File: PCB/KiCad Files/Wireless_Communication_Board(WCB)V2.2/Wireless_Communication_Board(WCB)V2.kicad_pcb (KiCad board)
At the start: 4 copper layers, 52.5 x 38.3 mm, 44 parts, among them J1 USB_B_Micro, J2 Power In, J3 Conn_01x04, J4 Conn_01x04, J5 Conn_01x04, J6 Conn_01x04, J7 Conn_01x04, Q2 UMH3N, U1 ESP32-PICO-MINI-02, U2 CP2102N-A02-GQFN28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

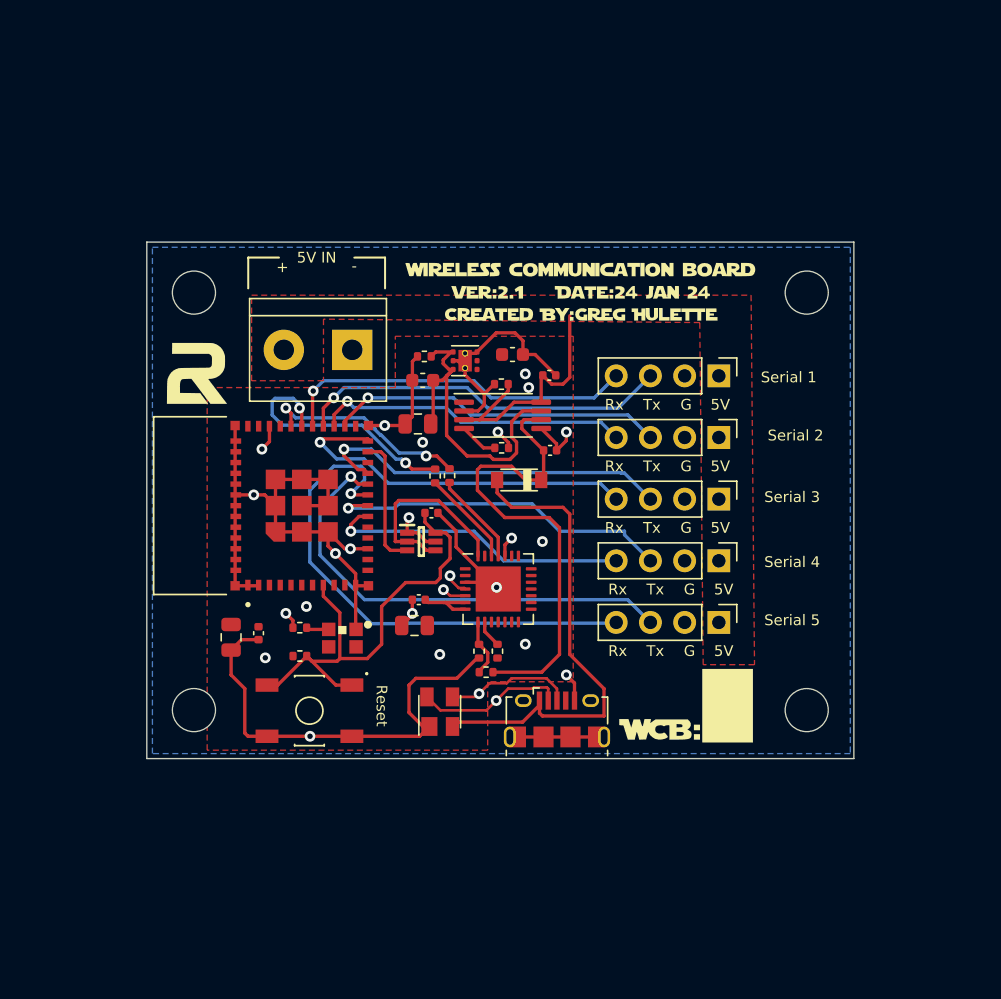
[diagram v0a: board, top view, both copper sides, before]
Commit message: Added WCB V2.2 and working on the code some.
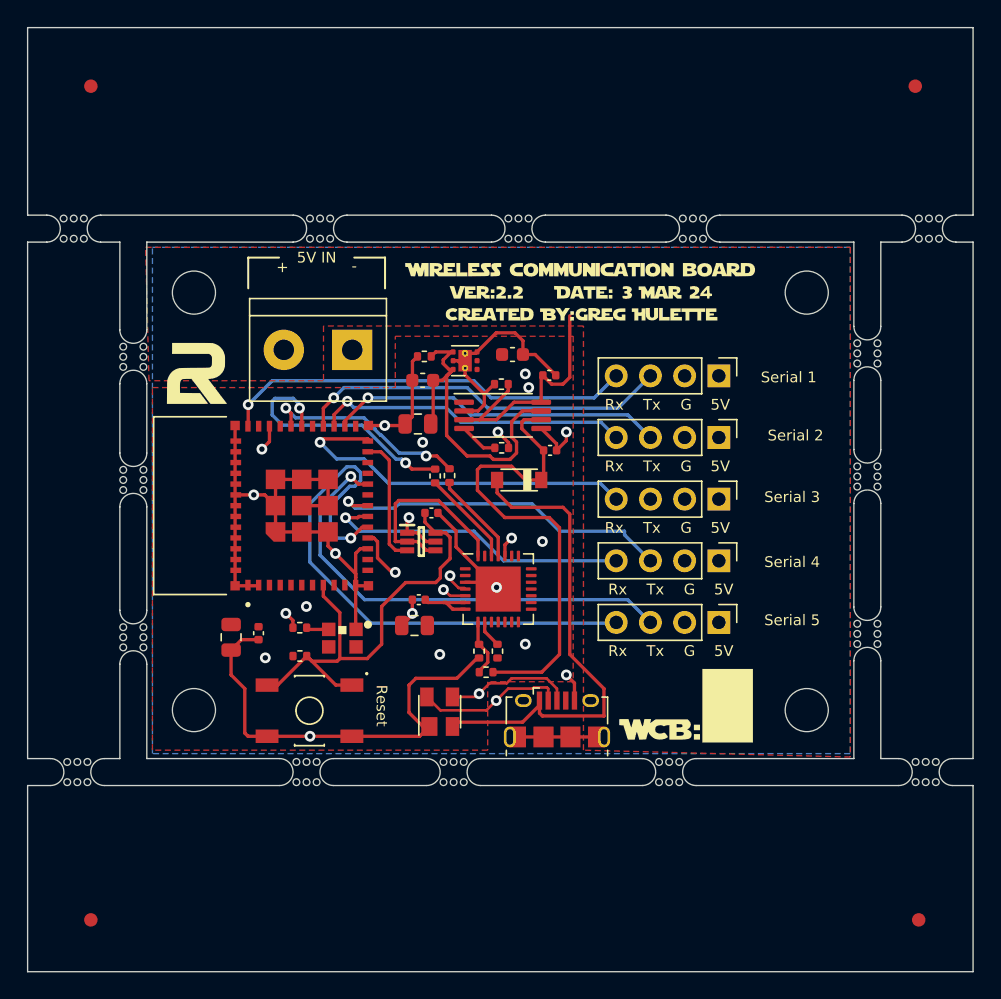
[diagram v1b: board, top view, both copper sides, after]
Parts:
- removed the G*** at (137.7, 91.4)
- added G***: LOGO, Logos:WCBv2.2Logo, F.Cu at (137.7, 91.4)
- added REF**: Fiducial_1mm_Mask2mm, Fiducial:Fiducial_1mm_Mask2mm, F.Cu at (101.3, 138.1)
- added REF**: Fiducial_1mm_Mask2mm, Fiducial:Fiducial_1mm_Mask2mm, F.Cu at (101.3, 76.2)
- added REF**: Fiducial_1mm_Mask2mm, Fiducial:Fiducial_1mm_Mask2mm, F.Cu at (162.6, 76.2)
- added REF**: Fiducial_1mm_Mask2mm, Fiducial:Fiducial_1mm_Mask2mm, F.Cu at (162.8, 138.1)
- added mouse-bite-2mm-slot: VAL**, Custom:mouse-bite-2mm-slot, F.Cu at (159.0, 96.0)
- added mouse-bite-2mm-slot: VAL**, Custom:mouse-bite-2mm-slot, F.Cu at (159.0, 105.2)
- added mouse-bite-2mm-slot: VAL**, Custom:mouse-bite-2mm-slot, F.Cu at (100.1, 86.8)
- added mouse-bite-2mm-slot: VAL**, Custom:mouse-bite-2mm-slot, F.Cu at (163.3, 127.1)
- added mouse-bite-2mm-slot: VAL**, Custom:mouse-bite-2mm-slot, F.Cu at (159.0, 116.8)
- added mouse-bite-2mm-slot: VAL**, Custom:mouse-bite-2mm-slot, F.Cu at (118.4, 86.8)
- added mouse-bite-2mm-slot: VAL**, Custom:mouse-bite-2mm-slot, F.Cu at (128.3, 127.1)
- added mouse-bite-2mm-slot: VAL**, Custom:mouse-bite-2mm-slot, F.Cu at (104.5, 117.1)
- added mouse-bite-2mm-slot: VAL**, Custom:mouse-bite-2mm-slot, F.Cu at (100.3, 127.1)
- added mouse-bite-2mm-slot: VAL**, Custom:mouse-bite-2mm-slot, F.Cu at (117.4, 127.1)
- added mouse-bite-2mm-slot: VAL**, Custom:mouse-bite-2mm-slot, F.Cu at (144.3, 127.1)
- added mouse-bite-2mm-slot: VAL**, Custom:mouse-bite-2mm-slot, F.Cu at (104.5, 96.3)
- added mouse-bite-2mm-slot: VAL**, Custom:mouse-bite-2mm-slot, F.Cu at (163.6, 86.8)
- added mouse-bite-2mm-slot: VAL**, Custom:mouse-bite-2mm-slot, F.Cu at (104.5, 105.4)
- added mouse-bite-2mm-slot: VAL**, Custom:mouse-bite-2mm-slot, F.Cu at (133.1, 86.8)
- added mouse-bite-2mm-slot: VAL**, Custom:mouse-bite-2mm-slot, F.Cu at (146.1, 86.8)
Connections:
- U1 pad 15: unconnected-(U1-Pad15) -> TX3
- U1 pad 16: unconnected-(U1-Pad16) -> RX5
- U1 pad 19: RX5 -> unconnected-(U1-Pad19)
- U1 pad 21: TX3 -> unconnected-(U1-Pad21)
- U1 pad 22: TX_HEADER -> unconnected-(U1-Pad22)
- U1 pad 29: RX1 -> unconnected-(U1-Pad29)
- U1 pad 35: unconnected-(U1-Pad35) -> RX1
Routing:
- net RX5: track 38.4 -> 42.9 mm
- net RX1: track 26.6 -> 30.9 mm
- net TX3: track 27.1 -> 25.0 mm
- net GND: track 122.6 -> 122.0 mm, vias 10 -> 9
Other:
- board size 52.5 x 38.3 mm -> 70.2 x 70.1 mm
